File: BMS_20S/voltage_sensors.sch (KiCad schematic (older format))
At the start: 27 parts, among them J401 VOLT_IDC_26_CONN

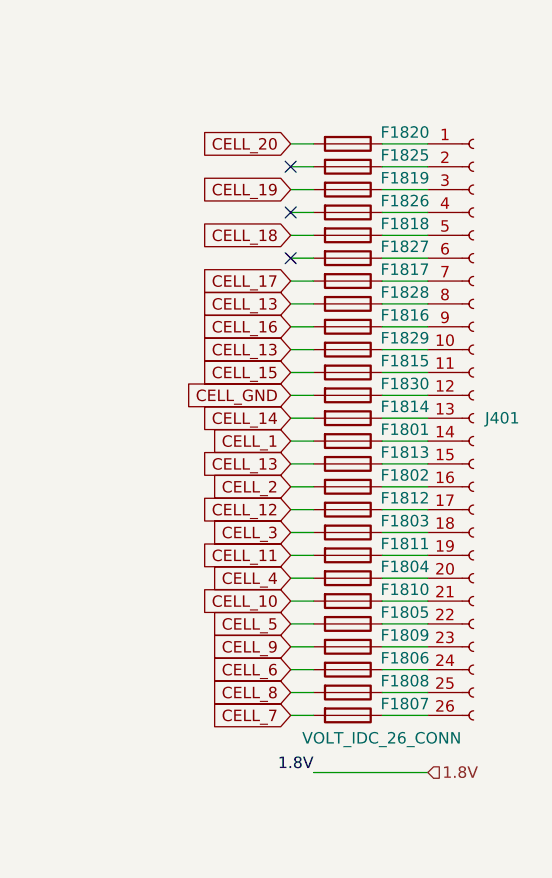
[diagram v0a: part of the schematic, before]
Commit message: add current sense block to the schematic
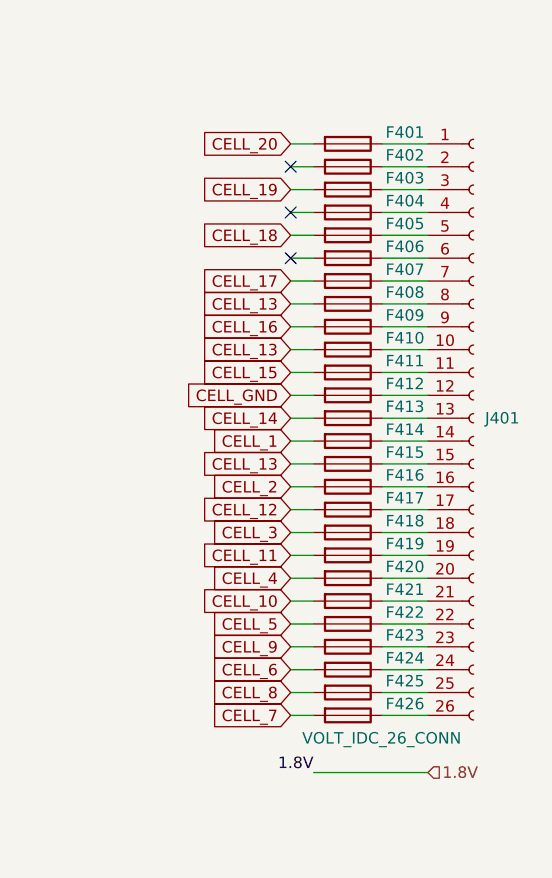
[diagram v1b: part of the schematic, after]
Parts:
- renumbered F1820 to F401, F1825 to F402, F1819 to F403, F1826 to F404, F1818 to F405, F1827 to F406, F1817 to F407, F1828 to F408, F1816 to F409, F1829 to F410, F1815 to F411, F1830 to F412, F1814 to F413, F1801 to F414, F1813 to F415, F1802 to F416, F1812 to F417, F1803 to F418, F1811 to F419, F1804 to F420, F1810 to F421, F1805 to F422, F1809 to F423, F1806 to F424, F1808 to F425, F1807 to F426
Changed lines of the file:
@@
 $Descr User 8268 5827
 encoding utf-8
-Sheet 4 31
+Sheet 4 32
 Title ""
 Date ""
@@
 	1000 1000 900  1000
 $Comp
-L Device:Fuse F1801
+L Device:Fuse F414
 U 1 1 5ECCCA3A
 P 6950 2400
-F 0 "F1801" V 6900 2650 50  0000 C CNN
+F 0 "F414" V 6900 2650 50  0000 C CNN
 F 1 "Fuse" V 6844 2400 50  0001 C CNN
 F 2 "e-Power:FUSE_1206_3216Metric" V 6880 2400 50  0001 C CNN
@@
 CELL_20
 $Comp
-L Device:Fuse F1802
+L Device:Fuse F416
 U 1 1 5ED10388
 P 6950 2600
-F 0 "F1802" V 6900 2850 50  0000 C CNN
+F 0 "F416" V 6900 2850 50  0000 C CNN
 F 1 "Fuse" V 6844 2600 50  0001 C CNN
 F 2 "e-Power:FUSE_1206_3216Metric" V 6880 2600 50  0001 C CNN
@@
 $EndComp
 $Comp
-L Device:Fuse F1804
+L Device:Fuse F420
 U 1 1 5ED10BA2
 P 6950 3000
-F 0 "F1804" V 6900 3250 50  0000 C CNN
+F 0 "F420" V 6900 3250 50  0000 C CNN
 F 1 "Fuse" V 6844 3000 50  0001 C CNN
 F 2 "e-Power:FUSE_1206_3216Metric" V 6880 3000 50  0001 C CNN
@@
 $EndComp
 $Comp
-L Device:Fuse F1805
+L Device:Fuse F422
 U 1 1 5ED10DC2
 P 6950 3200
-F 0 "F1805" V 6900 3450 50  0000 C CNN
+F 0 "F422" V 6900 3450 50  0000 C CNN
 F 1 "Fuse" V 6844 3200 50  0001 C CNN
 F 2 "e-Power:FUSE_1206_3216Metric" V 6880 3200 50  0001 C CNN
@@
 $EndComp
 $Comp
-L Device:Fuse F1806
+L Device:Fuse F424
 U 1 1 5ED10FE7
 P 6950 3400
-F 0 "F1806" V 6900 3650 50  0000 C CNN
+F 0 "F424" V 6900 3650 50  0000 C CNN
 F 1 "Fuse" V 6844 3400 50  0001 C CNN
 F 2 "e-Power:FUSE_1206_3216Metric" V 6880 3400 50  0001 C CNN
@@
 $EndComp
 $Comp
-L Device:Fuse F1807
+L Device:Fuse F426
 U 1 1 5ED1124E
 P 6950 3600
-F 0 "F1807" V 6900 3850 50  0000 C CNN
+F 0 "F426" V 6900 3850 50  0000 C CNN
 F 1 "Fuse" V 6844 3600 50  0001 C CNN
 F 2 "e-Power:FUSE_1206_3216Metric" V 6880 3600 50  0001 C CNN
@@
 $EndComp
 $Comp
-L Device:Fuse F1808
+L Device:Fuse F425
 U 1 1 5ED1148C
 P 6950 3500
-F 0 "F1808" V 6900 3750 50  0000 C CNN
+F 0 "F425" V 6900 3750 50  0000 C CNN
 F 1 "Fuse" V 6844 3500 50  0001 C CNN
 F 2 "e-Power:FUSE_1206_3216Metric" V 6880 3500 50  0001 C CNN
@@
 $EndComp
 $Comp
-L Device:Fuse F1809
+L Device:Fuse F423
 U 1 1 5ED116A7
 P 6950 3300
-F 0 "F1809" V 6900 3550 50  0000 C CNN
+F 0 "F423" V 6900 3550 50  0000 C CNN
 F 1 "Fuse" V 6844 3300 50  0001 C CNN
 F 2 "e-Power:FUSE_1206_3216Metric" V 6880 3300 50  0001 C CNN
@@
 $EndComp
 $Comp
-L Device:Fuse F1810
+L Device:Fuse F421
 U 1 1 5ED11921
 P 6950 3100
-F 0 "F1810" V 6900 3350 50  0000 C CNN
+F 0 "F421" V 6900 3350 50  0000 C CNN
 F 1 "Fuse" V 6844 3100 50  0001 C CNN
 F 2 "e-Power:FUSE_1206_3216Metric" V 6880 3100 50  0001 C CNN
@@
 $EndComp
 $Comp
-L Device:Fuse F1811
+L Device:Fuse F419
 U 1 1 5ED11B6F
 P 6950 2900
-F 0 "F1811" V 6900 3150 50  0000 C CNN
+F 0 "F419" V 6900 3150 50  0000 C CNN
 F 1 "Fuse" V 6844 2900 50  0001 C CNN
 F 2 "e-Power:FUSE_1206_3216Metric" V 6880 2900 50  0001 C CNN
@@
 $EndComp
 $Comp
-L Device:Fuse F1812
+L Device:Fuse F417
 U 1 1 5ED11DC0
 P 6950 2700
-F 0 "F1812" V 6900 2950 50  0000 C CNN
+F 0 "F417" V 6900 2950 50  0000 C CNN
 F 1 "Fuse" V 6844 2700 50  0001 C CNN
 F 2 "e-Power:FUSE_1206_3216Metric" V 6880 2700 50  0001 C CNN
@@
 $EndComp
 $Comp
-L Device:Fuse F1813
+L Device:Fuse F415
 U 1 1 5ED12065
 P 6950 2500
-F 0 "F1813" V 6900 2750 50  0000 C CNN
+F 0 "F415" V 6900 2750 50  0000 C CNN
 F 1 "Fuse" V 6844 2500 50  0001 C CNN
 F 2 "e-Power:FUSE_1206_3216Metric" V 6880 2500 50  0001 C CNN
@@
 $EndComp
 $Comp
-L Device:Fuse F1814
+L Device:Fuse F413
 U 1 1 5ED122D7
 P 6950 2300
-F 0 "F1814" V 6900 2550 50  0000 C CNN
+F 0 "F413" V 6900 2550 50  0000 C CNN
 F 1 "Fuse" V 6844 2300 50  0001 C CNN
 F 2 "e-Power:FUSE_1206_3216Metric" V 6880 2300 50  0001 C CNN
@@
 $EndComp
 $Comp
-L Device:Fuse F1815
+L Device:Fuse F411
 U 1 1 5ED1253C
 P 6950 2100
-F 0 "F1815" V 6900 2350 50  0000 C CNN
+F 0 "F411" V 6900 2350 50  0000 C CNN
 F 1 "Fuse" V 6844 2100 50  0001 C CNN
 F 2 "e-Power:FUSE_1206_3216Metric" V 6880 2100 50  0001 C CNN
@@
 $EndComp
 $Comp
-L Device:Fuse F1816
+L Device:Fuse F409
 U 1 1 5ED127A1
 P 6950 1900
-F 0 "F1816" V 6900 2150 50  0000 C CNN
+F 0 "F409" V 6900 2150 50  0000 C CNN
 F 1 "Fuse" V 6844 1900 50  0001 C CNN
 F 2 "e-Power:FUSE_1206_3216Metric" V 6880 1900 50  0001 C CNN
@@
 $EndComp
 $Comp
-L Device:Fuse F1817
+L Device:Fuse F407
 U 1 1 5ED12A06
 P 6950 1700
-F 0 "F1817" V 6900 1950 50  0000 C CNN
+F 0 "F407" V 6900 1950 50  0000 C CNN
 F 1 "Fuse" V 6844 1700 50  0001 C CNN
 F 2 "e-Power:FUSE_1206_3216Metric" V 6880 1700 50  0001 C CNN
@@
 $EndComp
 $Comp
-L Device:Fuse F1818
+L Device:Fuse F405
 U 1 1 5ED12C7D
 P 6950 1500
-F 0 "F1818" V 6900 1750 50  0000 C CNN
+F 0 "F405" V 6900 1750 50  0000 C CNN
 F 1 "Fuse" V 6844 1500 50  0001 C CNN
 F 2 "e-Power:FUSE_1206_3216Metric" V 6880 1500 50  0001 C CNN
@@
 $EndComp
 $Comp
-L Device:Fuse F1819
+L Device:Fuse F403
 U 1 1 5ED12F25
 P 6950 1300
-F 0 "F1819" V 6900 1550 50  0000 C CNN
+F 0 "F403" V 6900 1550 50  0000 C CNN
 F 1 "Fuse" V 6844 1300 50  0001 C CNN
 F 2 "e-Power:FUSE_1206_3216Metric" V 6880 1300 50  0001 C CNN
@@
 $EndComp
 $Comp
-L Device:Fuse F1820
+L Device:Fuse F401
 U 1 1 5ED1320D
 P 6950 1100
-F 0 "F1820" V 6900 1350 50  0000 C CNN
+F 0 "F401" V 6900 1350 50  0000 C CNN
 F 1 "Fuse" V 6844 1100 50  0001 C CNN
 F 2 "e-Power:FUSE_1206_3216Metric" V 6880 1100 50  0001 C CNN
@@
 $EndComp
 $Comp
-L Device:Fuse F1825
+L Device:Fuse F402
 U 1 1 5ED13EB3
 P 6950 1200
-F 0 "F1825" V 6900 1450 50  0000 C CNN
+F 0 "F402" V 6900 1450 50  0000 C CNN
 F 1 "Fuse" V 6844 1200 50  0001 C CNN
 F 2 "e-Power:FUSE_1206_3216Metric" V 6880 1200 50  0001 C CNN
@@
 $EndComp
 $Comp
-L Device:Fuse F1826
+L Device:Fuse F404
 U 1 1 5ED141BF
 P 6950 1400
-F 0 "F1826" V 6900 1650 50  0000 C CNN
+F 0 "F404" V 6900 1650 50  0000 C CNN
 F 1 "Fuse" V 6844 1400 50  0001 C CNN
 F 2 "e-Power:FUSE_1206_3216Metric" V 6880 1400 50  0001 C CNN
@@
 $EndComp
 $Comp
-L Device:Fuse F1827
+L Device:Fuse F406
 U 1 1 5ED14362
 P 6950 1600
-F 0 "F1827" V 6900 1850 50  0000 C CNN
+F 0 "F406" V 6900 1850 50  0000 C CNN
 F 1 "Fuse" V 6844 1600 50  0001 C CNN
 F 2 "e-Power:FUSE_1206_3216Metric" V 6880 1600 50  0001 C CNN
@@
 $EndComp
 $Comp
-L Device:Fuse F1828
+L Device:Fuse F408
 U 1 1 5ED1460F
 P 6950 1800
-F 0 "F1828" V 6900 2050 50  0000 C CNN
+F 0 "F408" V 6900 2050 50  0000 C CNN
 F 1 "Fuse" V 6844 1800 50  0001 C CNN
 F 2 "e-Power:FUSE_1206_3216Metric" V 6880 1800 50  0001 C CNN
@@
 $EndComp
 $Comp
-L Device:Fuse F1829
+L Device:Fuse F410
 U 1 1 5ED14893
 P 6950 2000
-F 0 "F1829" V 6900 2250 50  0000 C CNN
+F 0 "F410" V 6900 2250 50  0000 C CNN
 F 1 "Fuse" V 6844 2000 50  0001 C CNN
 F 2 "e-Power:FUSE_1206_3216Metric" V 6880 2000 50  0001 C CNN
@@
 	7100 2400 7300 2400
 $Comp
-L Device:Fuse F1830
+L Device:Fuse F412
 U 1 1 5ED8D5B9
 P 6950 2200
-F 0 "F1830" V 6900 2450 50  0000 C CNN
+F 0 "F412" V 6900 2450 50  0000 C CNN
 F 1 "Fuse" V 6844 2200 50  0001 C CNN
 F 2 "e-Power:FUSE_1206_3216Metric" V 6880 2200 50  0001 C CNN
@@
 	7100 2600 7300 2600
 $Comp
-L Device:Fuse F1803
+L Device:Fuse F418
 U 1 1 5ED10754
 P 6950 2800
-F 0 "F1803" V 6900 3050 50  0000 C CNN
+F 0 "F418" V 6900 3050 50  0000 C CNN
 F 1 "Fuse" V 6844 2800 50  0001 C CNN
 F 2 "e-Power:FUSE_1206_3216Metric" V 6880 2800 50  0001 C CNN
